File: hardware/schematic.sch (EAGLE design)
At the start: 30 parts, among them X1 SMA-142-0701-801/806

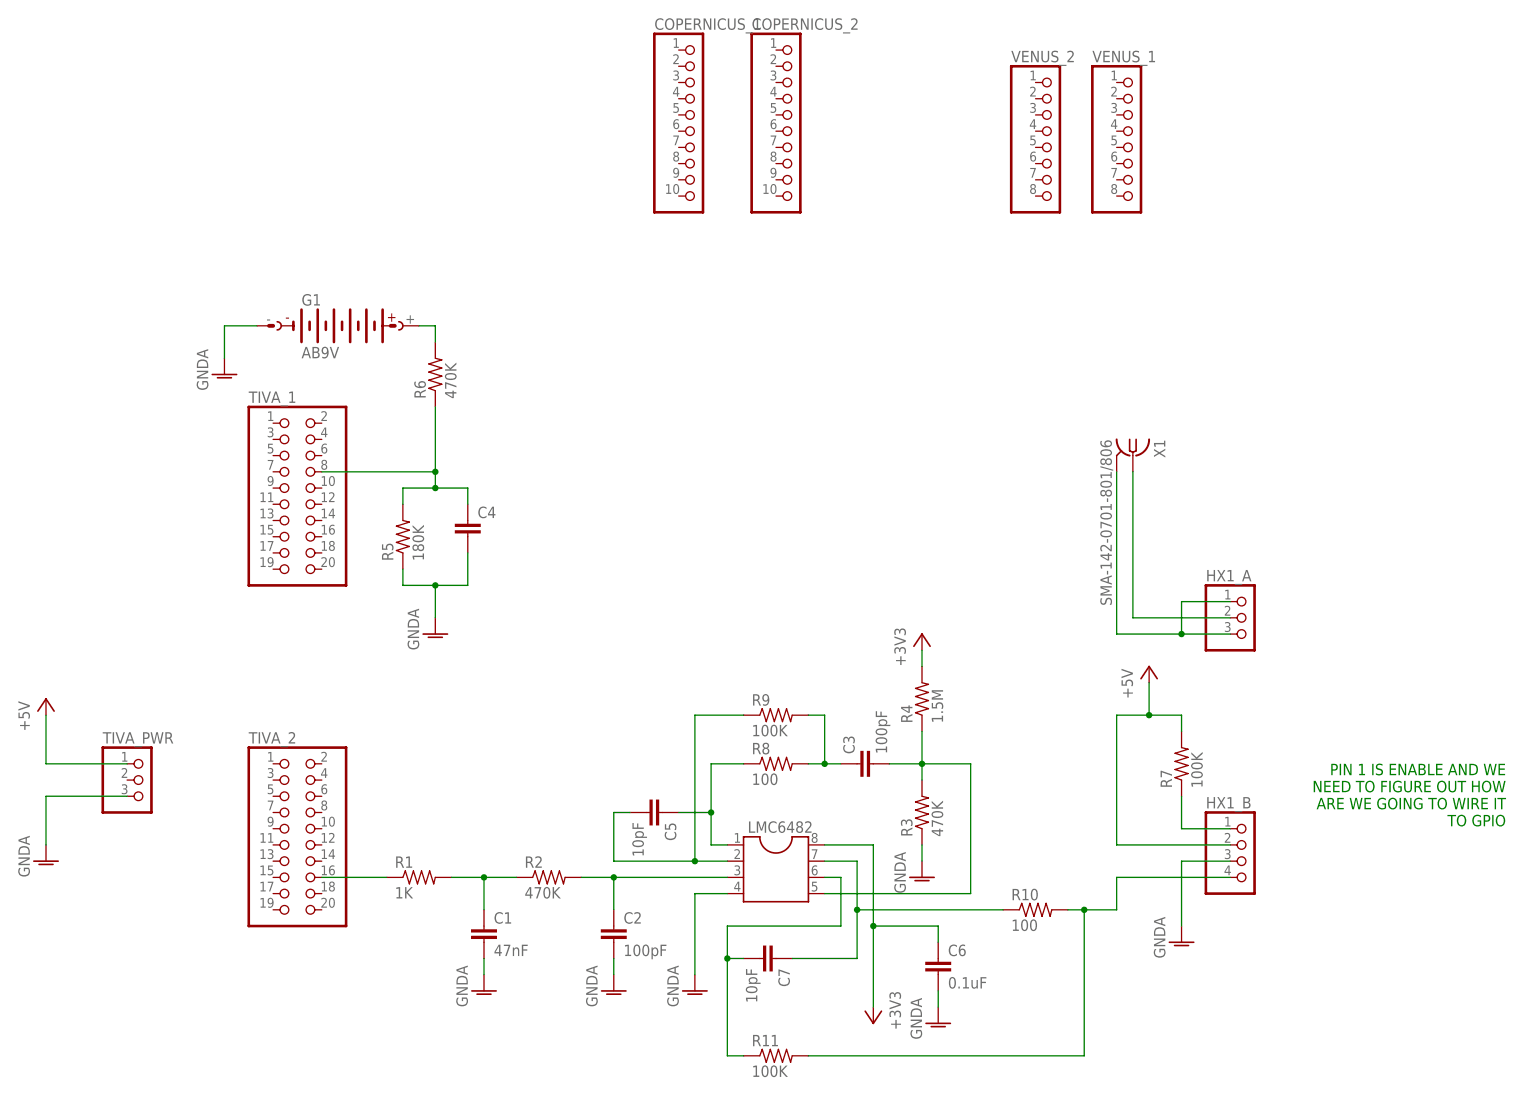
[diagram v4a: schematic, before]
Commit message: My first take on the complete PCB (if we want to make it). No vias, traces on one side only (+ ground plane), should dimensionally match the Tiva (1::1 print to make sure!)
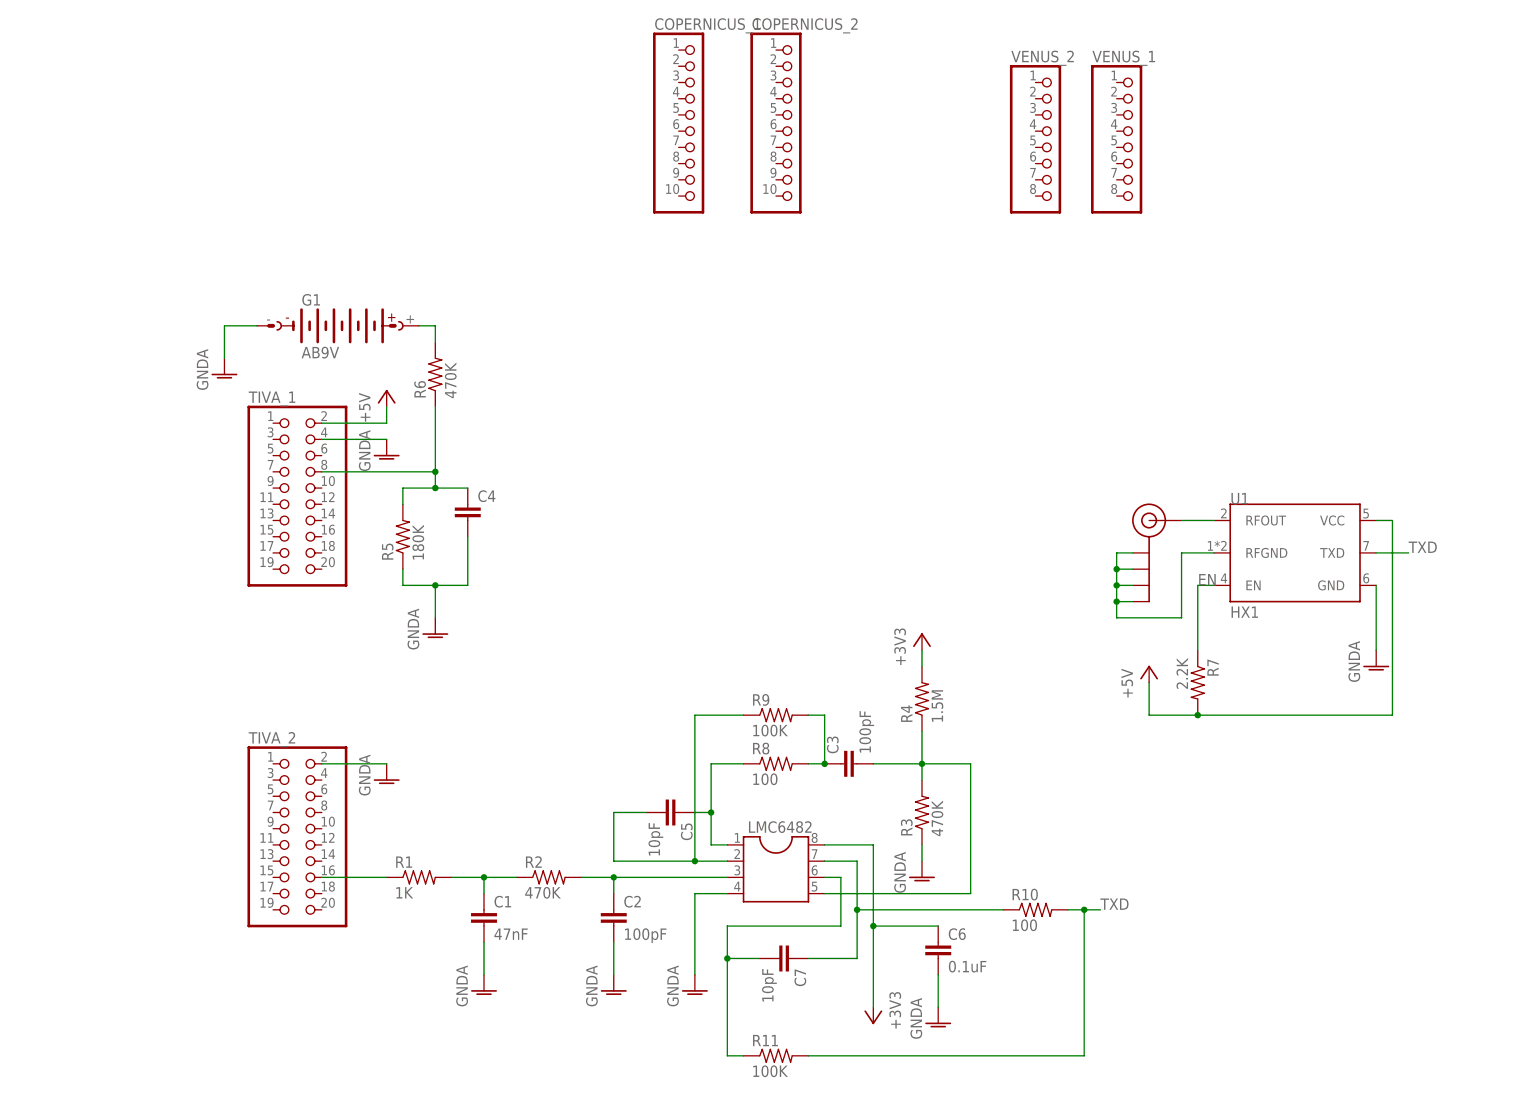
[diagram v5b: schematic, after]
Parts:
- removed HX1_A, TIVA_PWR: (no value), pinhead:PINHD-1X3
- removed HX1_B: (no value), pinhead:PINHD-1X4
- removed X1: SMA-142-0701-801/806, con-coax:SMA-142-0701-801/806
- added J1: SMA_EDGE, SparkFun-Connectors:SMA_EDGE
- added U1: HX1, HAB:HX1
- C1, C2, C3, C4, C5, C6, C7: device capacitor-wima:C2.5/2 -> SparkFun-Passives:CAP1206
- R1, R10, R11, R2, R3, R4, R5, R6, R8, R9: device resistor:R-US_0204/2V -> SparkFun-Passives:RESISTOR1206
- R7: value 100K -> 2.2K; device resistor:R-US_0204/2V -> SparkFun-Passives:RESISTOR1206
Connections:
- net N$1 renamed PWMOUT
- net N$10 renamed +9V
- net N$12 renamed TXF
- net N$13 renamed LPOUT
- net N$15 renamed LPFB
- net N$2 renamed PWMF1
- net N$3 renamed PWMF2
- net N$4 renamed HPFB
- net N$6 renamed HPOUT
- net N$8 renamed HPIN
- net N$9 renamed VBAT
- removed net N$11: HX1_B.1, R7.1
- removed net N$14: HX1_B.4, R10.2, R11.2
- removed net N$5: HX1_A.1, HX1_A.3, X1.2
- removed net N$7: HX1_A.2, X1.1
- new net EN: R7.1, U1.EN
- new net RFGND: J1.GND@0, J1.GND@1, J1.GND@2, J1.GND@3, U1.RFGND
- new net RFOUT: J1.SIGNAL, U1.RFOUT
- new net TXD: R10.2, R11.2, U1.TXD
- net +5V: now also TIVA_1.2, U1.VCC; no longer HX1_B.2, TIVA_PWR.1
- net GNDA: now also TIVA_1.4, TIVA_2.2, U1.GND; no longer HX1_B.3, TIVA_PWR.3
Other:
- note removed: "PIN 1 IS ENABLE AND WE NEED TO FIGURE OUT HOW ARE WE GOING TO WIRE IT TO GPIO"
- moved on the sheet: C1, C2, C3, C4, C5, C6, C7, R7
